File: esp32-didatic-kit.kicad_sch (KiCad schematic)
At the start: 0 parts

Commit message: add MCU + output
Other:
- added sheet IO (sheets/io.kicad_sch)
- added sheet MCU (sheets/mcu.kicad_sch)

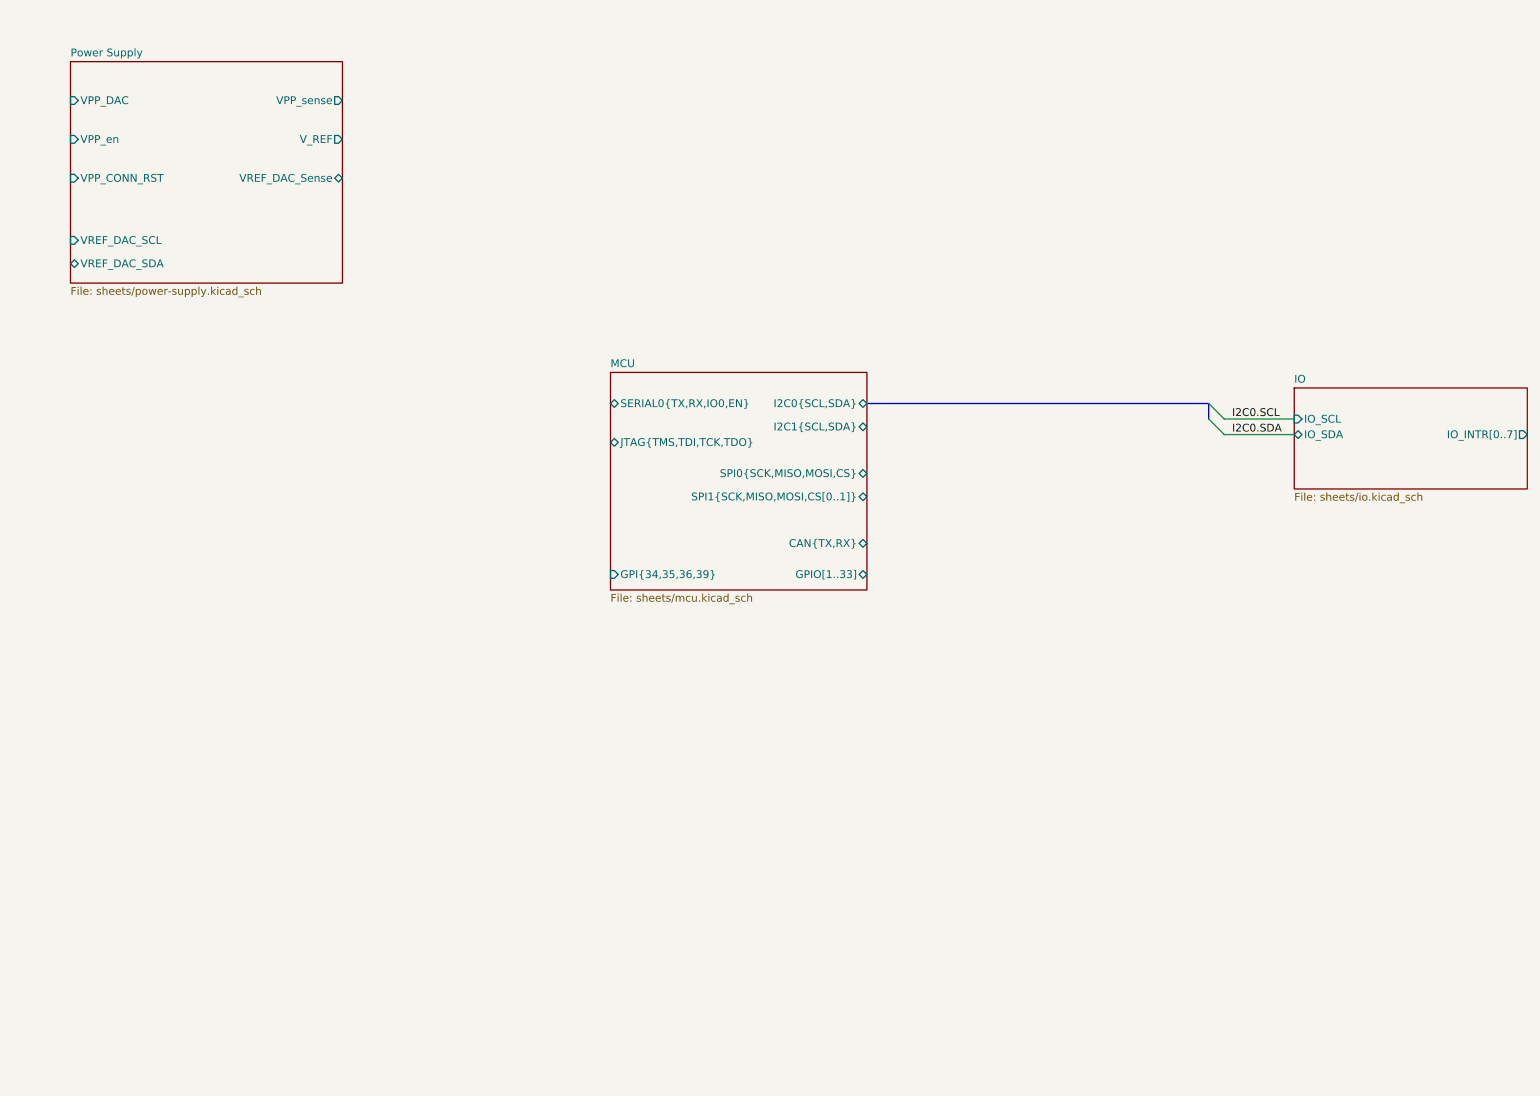
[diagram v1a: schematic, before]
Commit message: add mcu module + position components
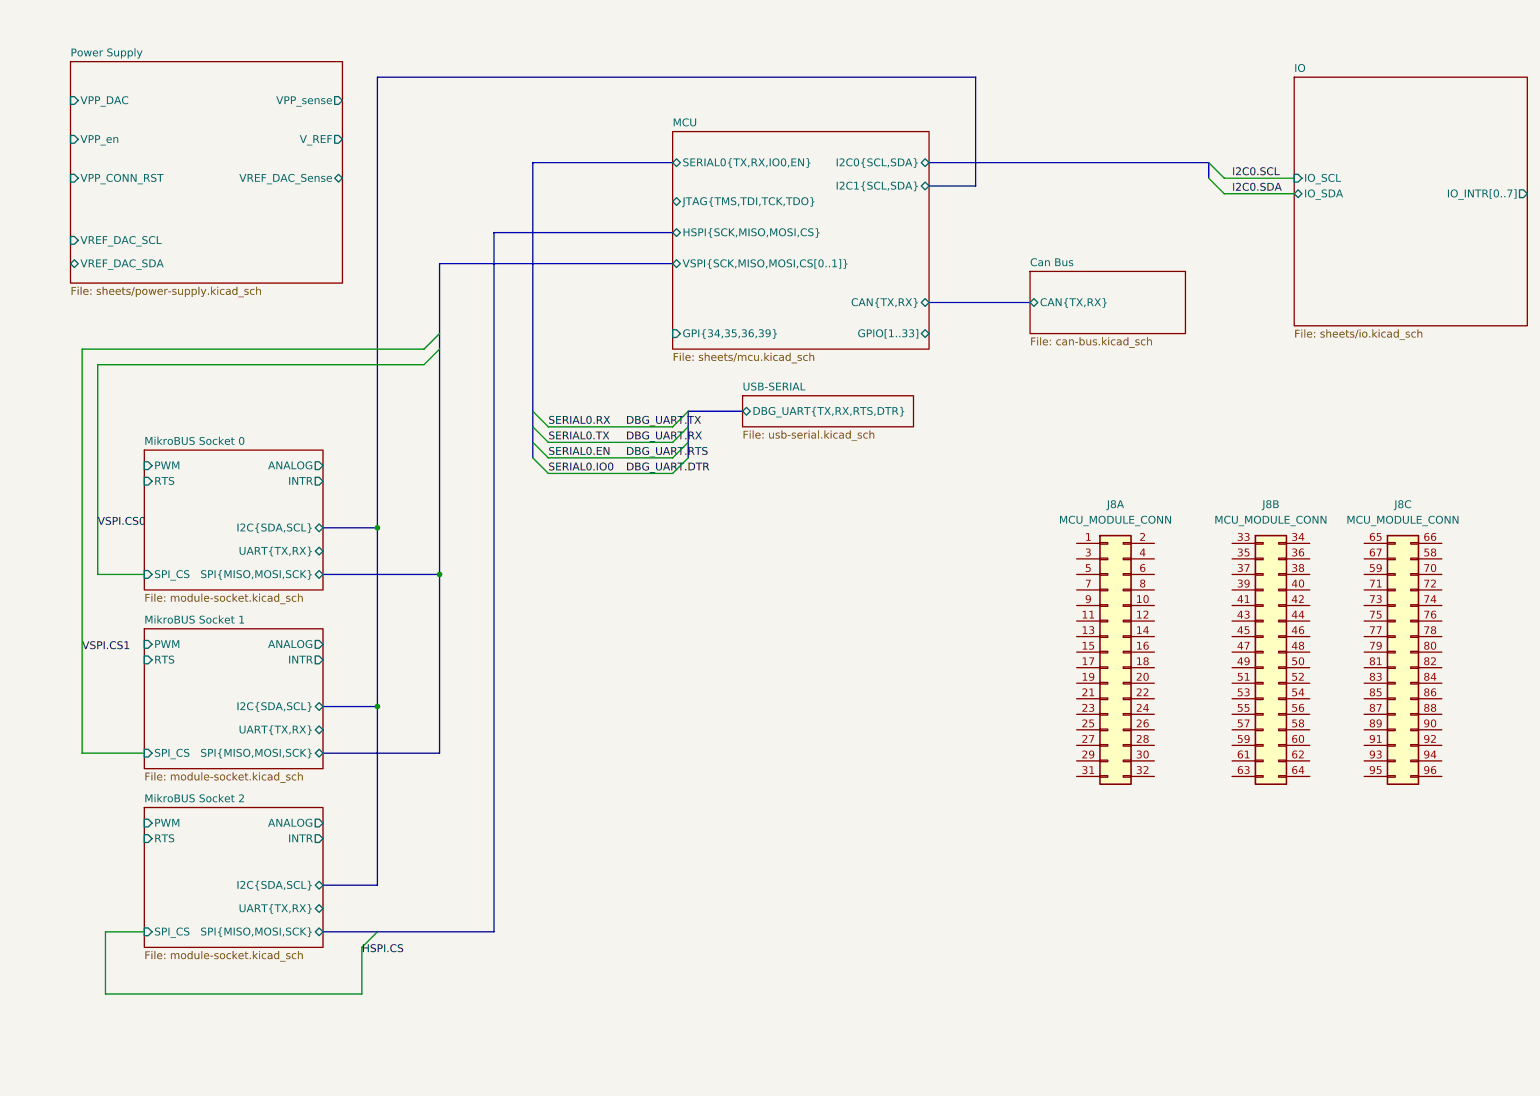
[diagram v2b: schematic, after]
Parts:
- added J8: MCU_MODULE_CONN, Connectors:mcu_conn, symbol Connectors:MCU_MODULE_CONN
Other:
- added sheet Can Bus (can-bus.kicad_sch)
- added sheet MikroBUS Socket 0 (module-socket.kicad_sch)
- added sheet MikroBUS Socket 1 (module-socket.kicad_sch)
- added sheet MikroBUS Socket 2 (module-socket.kicad_sch)
- added sheet USB-SERIAL (usb-serial.kicad_sch)
- sheet MCU ports: added HSPI{SCK,MISO,MOSI,CS}, VSPI{SCK,MISO,MOSI,CS[0..1]}; removed SPI0{SCK,MISO,MOSI,CS}, SPI1{SCK,MISO,MOSI,CS[0..1]}

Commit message: Updated MCU to MCU module + set SMD comp. footprints
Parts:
- removed J8: MCU_MODULE_CONN, Connectors:mcu_conn, symbol Connectors:MCU_MODULE_CONN
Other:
- sheet MCU ports: added PA[0..7], PB[0..7]; removed none

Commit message: add PA an PB ports
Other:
- sheet IO ports: added PA[0..7], PB[0..7]; removed none
- sheet MCU ports: added none; removed GPIO[1..33]
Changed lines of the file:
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@@
 	(bus
 		(pts
-			(xy 172.72 64.77) (xy 189.23 64.77)
+			(xy 180.34 116.84) (xy 187.96 116.84)
 		)
 		(stroke
@@
 	(bus
 		(pts
+			(xy 172.72 49.53) (xy 232.41 49.53)
+		)
+		(stroke
+			(width 0)
+			(type default)
+		)
+	)
+	(bus
+		(pts
 			(xy 172.72 45.72) (xy 180.34 45.72)
 		)
@@
 		)
 	)
+	(bus
+		(pts
+			(xy 180.34 64.77) (xy 180.34 116.84)
+		)
+		(stroke
+			(width 0)
+			(type default)
+		)
+	)
 	(wire
 		(pts
@@
 		)
 	)
+	(bus
+		(pts
+			(xy 180.34 64.77) (xy 172.72 64.77)
+		)
+		(stroke
+			(width 0)
+			(type default)
+		)
+	)
 	(wire
 		(pts
@@
 		(pts
 			(xy 34.29 72.39) (xy 34.29 138.43)
+		)
+		(stroke
+			(width 0)
+			(type default)
+		)
+	)
+	(bus
+		(pts
+			(xy 172.72 53.34) (xy 232.41 53.34)
 		)
 		(stroke
@@
 	)
 	(sheet
-		(at 189.23 59.69)
+		(at 187.96 111.76)
 		(size 25.4 10.16)
 		(exclude_from_sim no)
@@
 		)
 		(property "Sheetname" "Can Bus"
-			(at 189.23 58.9784 0)
+			(at 187.96 111.0484 0)
 			(effects
 				(font
@@
 		)
 		(property "Sheetfile" "can-bus.kicad_sch"
-			(at 189.23 70.4346 0)
+			(at 187.96 122.5046 0)
 			(effects
 				(font
@@
 		)
 		(pin "CAN{TX,RX}" bidirectional
-			(at 189.23 64.77 180)
+			(at 187.96 116.84 180)
 			(effects
 				(font
@@
 			)
 		)
+		(pin "PA[0..7]" input
+			(at 232.41 49.53 180)
+			(effects
+				(font
+					(size 1.27 1.27)
+				)
+				(justify left)
+			)
+		)
+		(pin "PB[0..7]" input
+			(at 232.41 53.34 180)
+			(effects
+				(font
+					(size 1.27 1.27)
+				)
+				(justify left)
+			)
+		)
 		(instances
 			(project "esp32-didatic-kit"
@@
 			)
 		)
-		(pin "GPIO[1..33]" bidirectional
-			(at 172.72 69.85 0)
-			(effects
-				(font
-					(size 1.27 1.27)
-				)
-				(justify right)
-			)
-		)

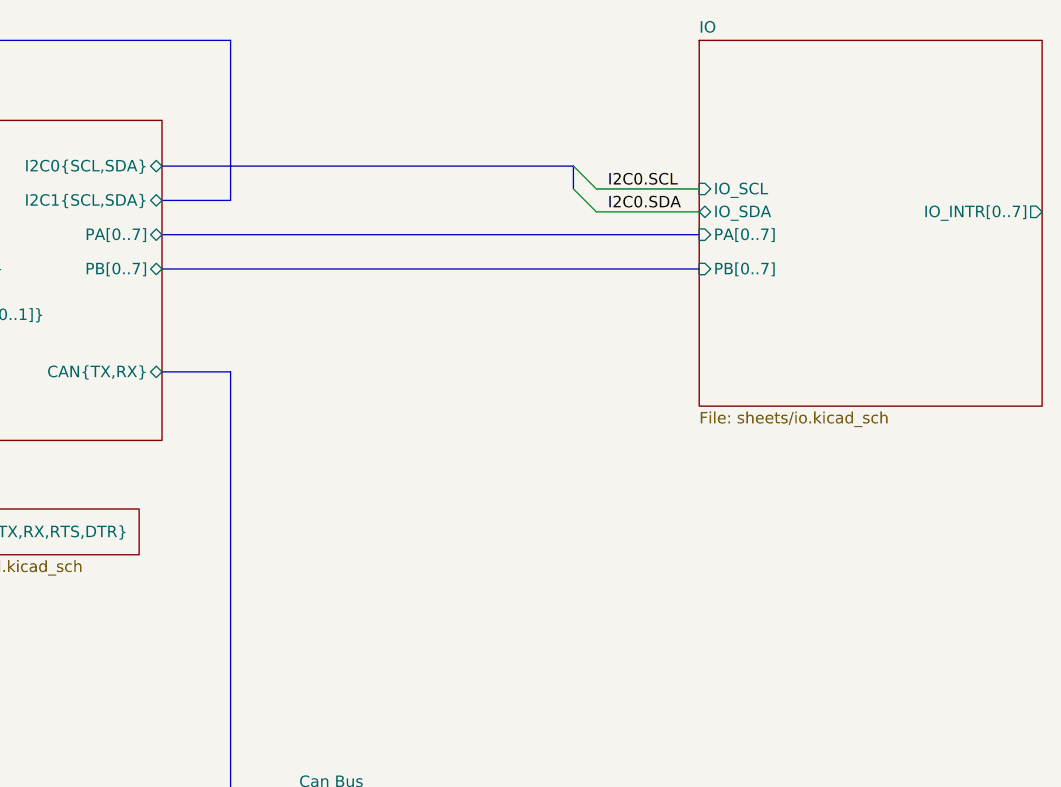
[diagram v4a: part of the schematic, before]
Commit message: updated silk + started routing
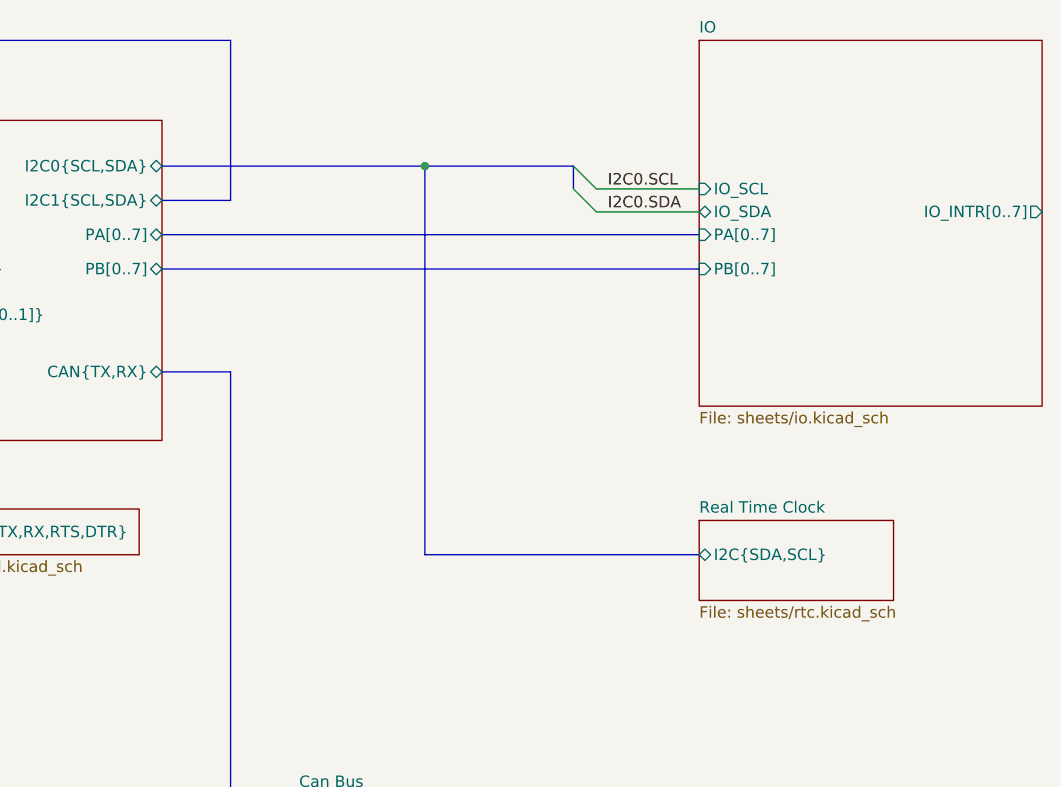
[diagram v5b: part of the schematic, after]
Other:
- added sheet Real Time Clock (sheets/rtc.kicad_sch)
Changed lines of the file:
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@@
 	(paper "A4")
+	(junction
+		(at 201.93 41.91)
+		(diameter 0)
+		(color 0 0 0 0)
+	)
 	(junction
 		(at 82.55 130.81)
@@
 	(bus
 		(pts
+			(xy 232.41 85.09) (xy 201.93 85.09)
+		)
+		(stroke
+			(width 0)
+			(type default)
+		)
+	)
+	(bus
+		(pts
 			(xy 180.34 27.94) (xy 82.55 27.94)
 		)
@@
 	(bus
 		(pts
+			(xy 201.93 41.91) (xy 218.44 41.91)
+		)
+		(stroke
+			(width 0)
+			(type default)
+		)
+	)
+	(bus
+		(pts
 			(xy 172.72 45.72) (xy 180.34 45.72)
 		)
@@
 	(bus
 		(pts
-			(xy 172.72 41.91) (xy 218.44 41.91)
+			(xy 172.72 41.91) (xy 201.93 41.91)
 		)
 		(stroke
@@
 		(pts
 			(xy 220.98 44.45) (xy 232.41 44.45)
+		)
+		(stroke
+			(width 0)
+			(type default)
+		)
+	)
+	(bus
+		(pts
+			(xy 201.93 85.09) (xy 201.93 41.91)
 		)
 		(stroke
@@
 		)
 	)
+	(sheet
+		(at 232.41 81.28)
+		(size 21.59 8.89)
+		(exclude_from_sim no)
+		(in_bom yes)
+		(on_board yes)
+		(dnp no)
+		(fields_autoplaced yes)
+		(stroke
+			(width 0.1524)
+			(type solid)
+		)
+		(fill
+			(color 0 0 0 0.0000)
+		)
+		(property "Sheetname" "Real Time Clock"
+			(at 232.41 80.5684 0)
+			(effects
+				(font
+					(size 1.27 1.27)
+				)
+				(justify left bottom)
+			)
+		)
+		(property "Sheetfile" "sheets/rtc.kicad_sch"
+			(at 232.41 90.7546 0)
+			(effects
+				(font
+					(size 1.27 1.27)
+				)
+				(justify left top)
+			)
+		)
+		(pin "I2C{SDA,SCL}" bidirectional
+			(at 232.41 85.09 180)
+			(effects
+				(font
+					(size 1.27 1.27)
+				)
+				(justify left)
+			)
+		)
+		(instances
+			(project "esp32-didatic-kit"
+				(path "/f57920a5-fee7-4fe5-a133-e8b36941a5a6"
+					(page "57")
+				)
+			)
+		)
+	)

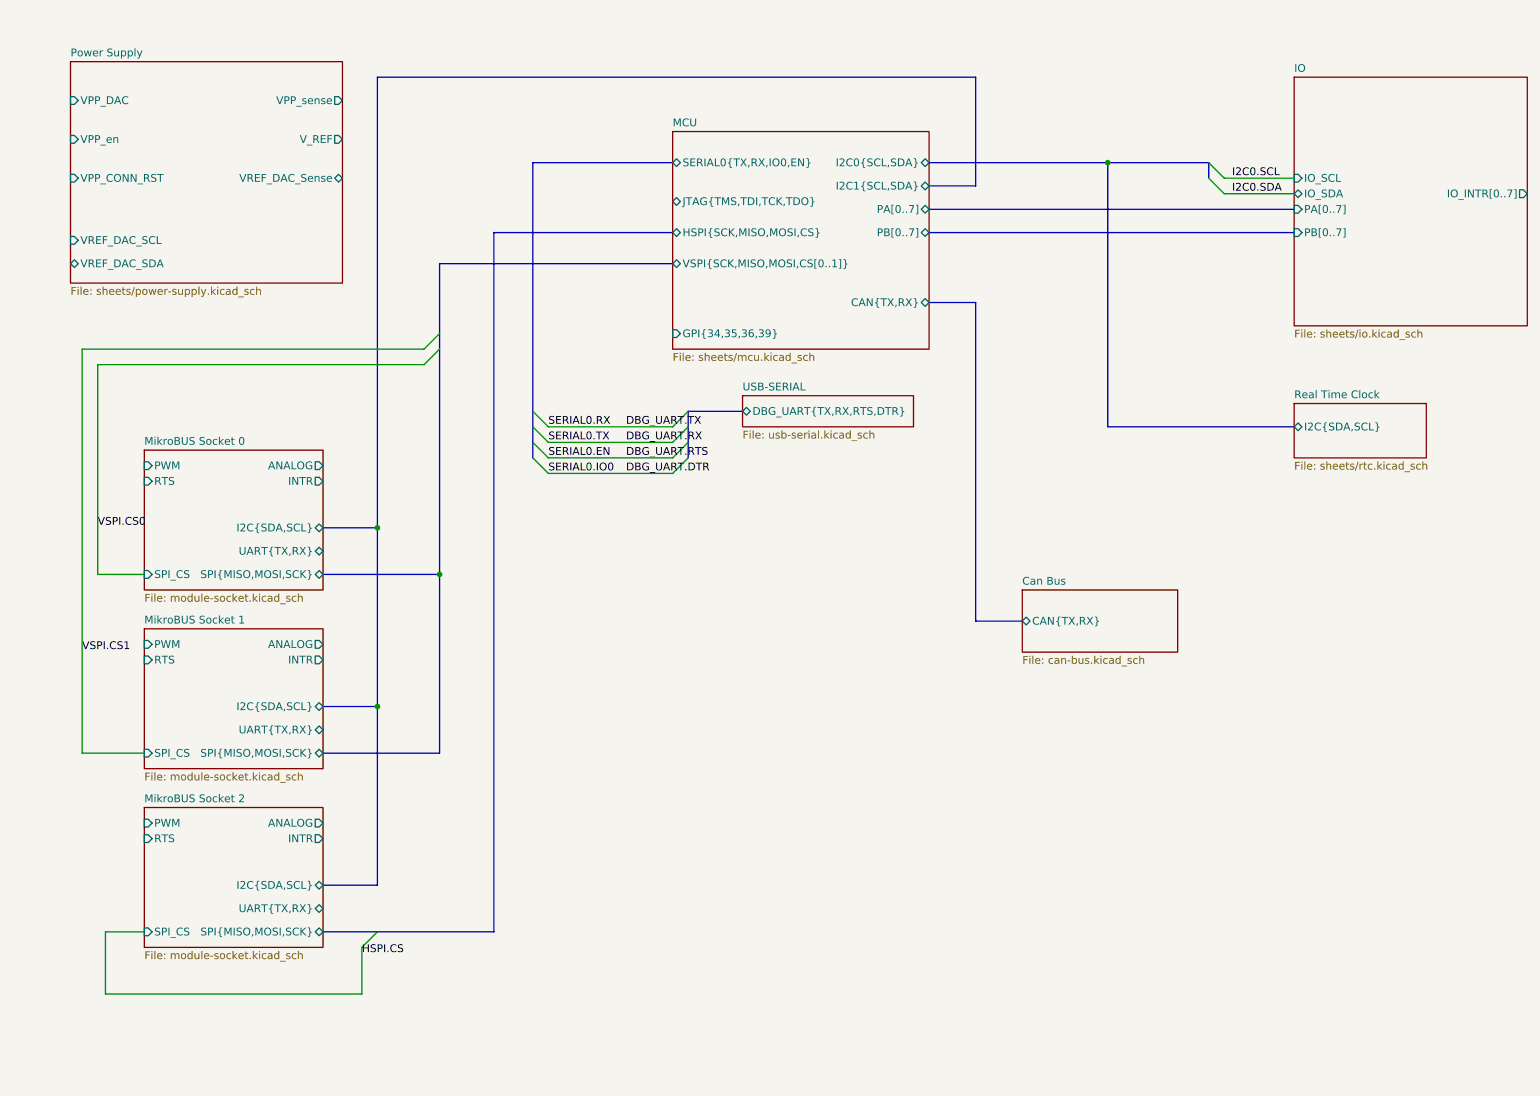
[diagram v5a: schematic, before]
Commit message: finished routing SPI, I2C and MikroBUS
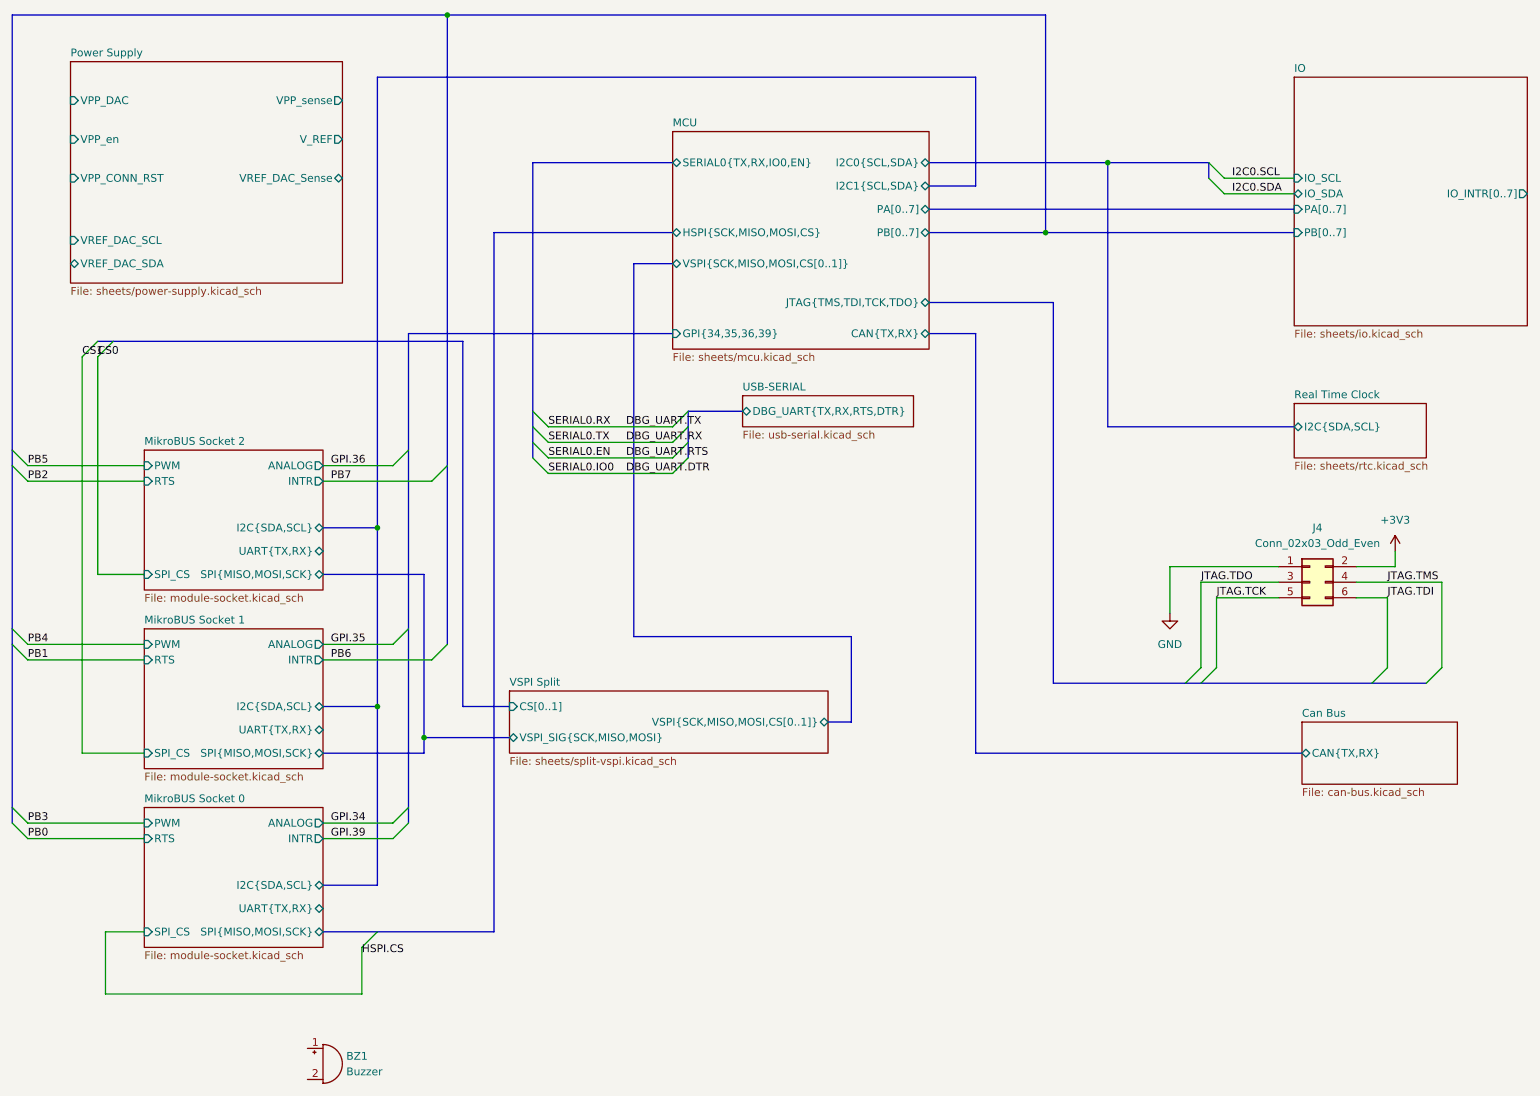
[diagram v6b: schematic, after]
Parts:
- added BZ1: Buzzer, symbol Device:Buzzer
- added J4: Conn_02x03_Odd_Even, Connector_PinSocket_2.54mm:PinSocket_2x03_P2.54mm_Vertical, symbol Connector_Generic:Conn_02x03_Odd_Even
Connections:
- new net +3V3: J4.2 (Pin_2)
- new net GND: J4.1 (Pin_1)
- new net JTAG.TCK: J4.5 (Pin_5)
- new net JTAG.TDI: J4.6 (Pin_6)
- new net JTAG.TDO: J4.3 (Pin_3)
- new net JTAG.TMS: J4.4 (Pin_4)
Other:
- added sheet VSPI Split (sheets/split-vspi.kicad_sch)
